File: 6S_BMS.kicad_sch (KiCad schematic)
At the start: 42 parts, among them J1 Conn_01x08_Pin, J4 Conn_01x02_Pin, J5 Conn_01x04_Pin, J6 Conn_01x04_Pin, SW1 SW_SPST, U1 BQ76925RGER, U2 STM32L431KCUx, U3 TJA1051TK-3, U4 TCAN3404DRBRQ1

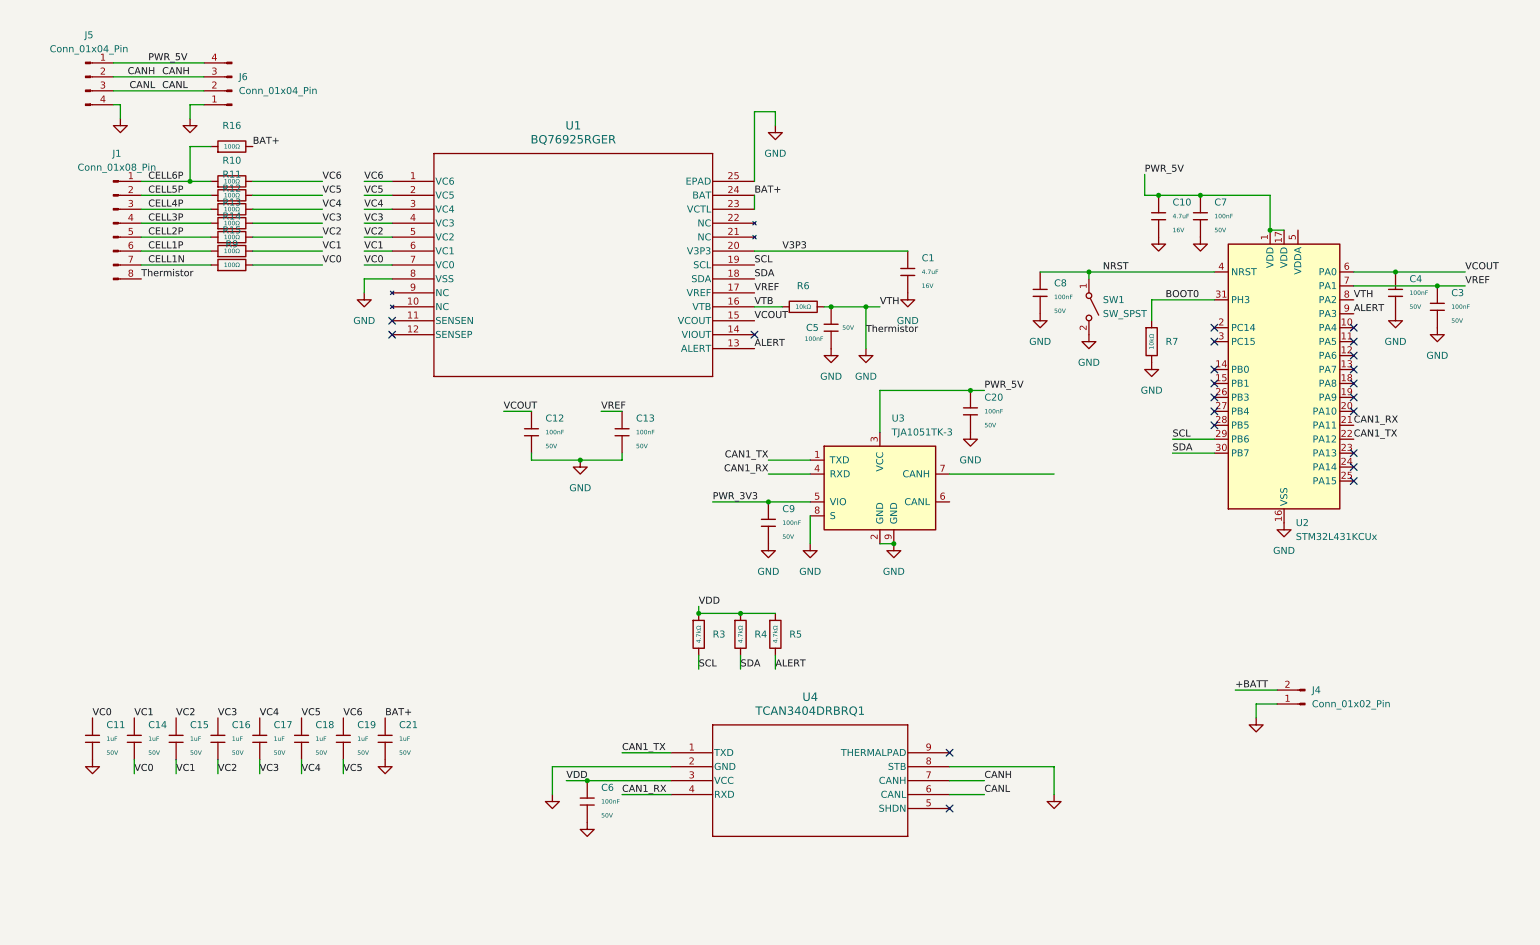
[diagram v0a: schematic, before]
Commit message: Added component properties, updated CAN loop
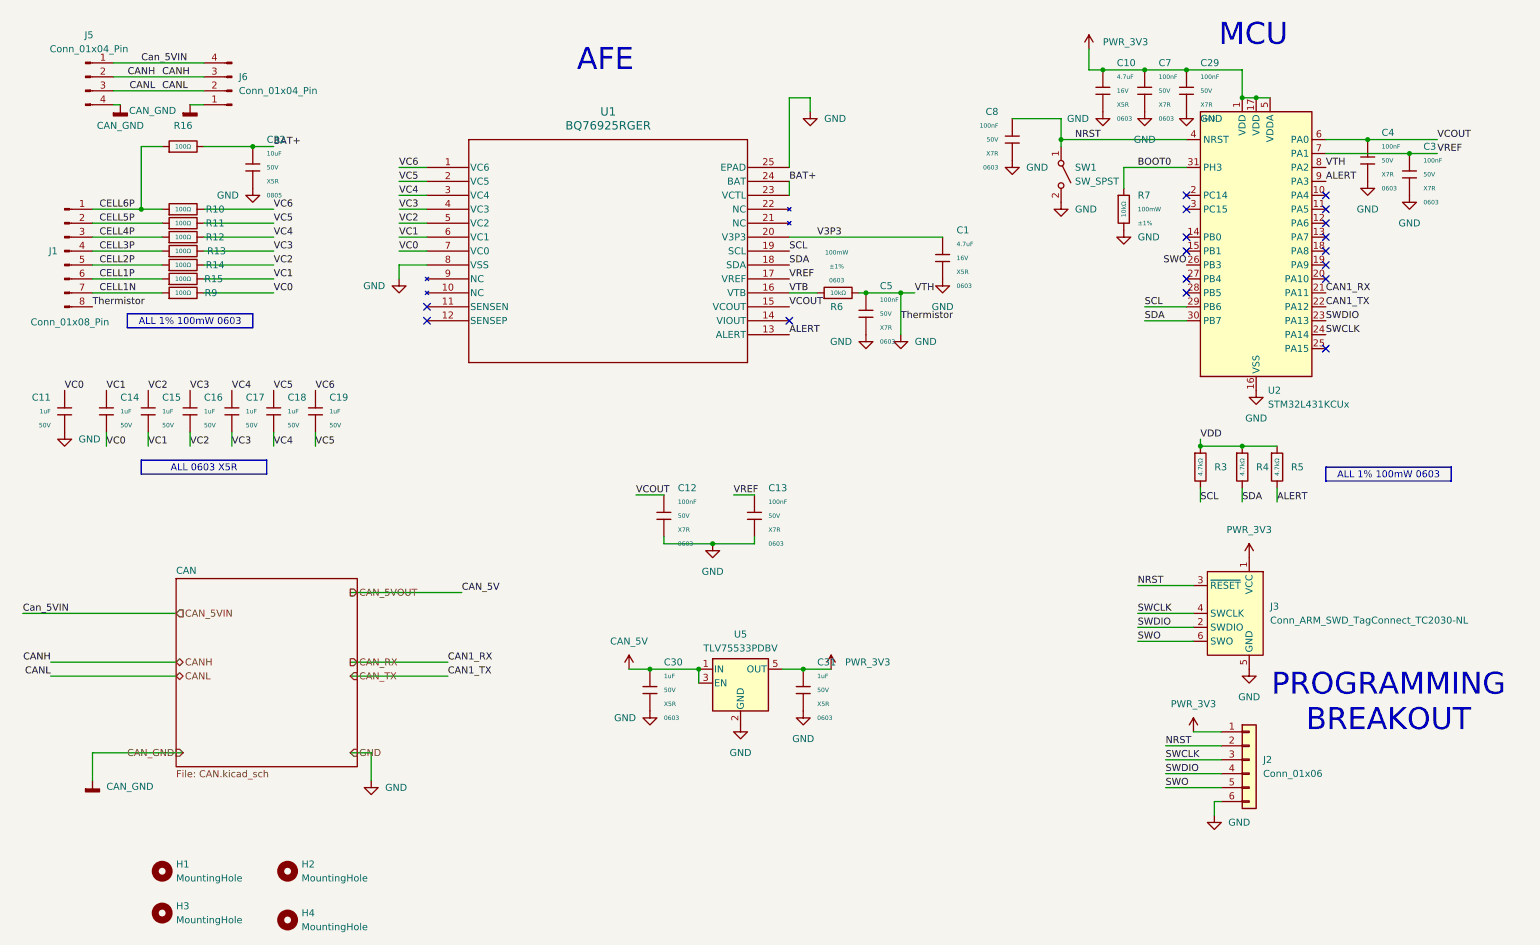
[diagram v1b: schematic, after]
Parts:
- removed C20, C6, C9: 100nF, PCM_JLCPCB:C_0603, symbol PCM_JLCPCB-Capacitors:0603,100nF
- removed C21: 1uF, PCM_JLCPCB:C_0603, symbol PCM_JLCPCB-Capacitors:0603,1uF
- removed J4: Conn_01x02_Pin, symbol Connector:Conn_01x02_Pin
- removed U3: TJA1051TK-3, Package_DFN_QFN:DFN-8-1EP_3x3mm_P0.65mm_EP1.55x2.4mm, symbol Interface_CAN_LIN:TJA1051TK-3
- removed U4: TCAN3404DRBRQ1, TCAN:SON8_DRB_TEX, symbol 2026-03-12_01-27-55:TCAN3404DRBRQ1
- added C29: 100nF, PCM_JLCPCB:C_0603, symbol PCM_JLCPCB-Capacitors:0603,100nF
- added C30, C31: 1uF, PCM_JLCPCB:C_0603, symbol PCM_JLCPCB-Capacitors:0603,1uF
- added C32: 10uF, PCM_JLCPCB:C_0805, symbol PCM_JLCPCB-Capacitors:0805,10uF,(2)
- added H1, H2, H3, H4: MountingHole, symbol Mechanical:MountingHole
- added J2: Conn_01x06, symbol Connector_Generic:Conn_01x06
- added J3: Conn_ARM_SWD_TagConnect_TC2030-NL, Connector:Tag-Connect_TC2030-IDC-NL_2x03_P1.27mm_Vertical, symbol Connector:Conn_ARM_SWD_TagConnect_TC2030-NL
- added U5: TLV75533PDBV, Package_TO_SOT_SMD:SOT-23-5, symbol Regulator_Linear:TLV75533PDBV
- C1, C10, C12, C13, C3, C4, C5, C7, C8, R6: Package (none) -> 0603
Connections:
- net BAT+: now also C32.1
- net GND: now also C29.1, C30.2, C31.2, C32.2, J2.6 (Pin_6), J3.5 (GND), U5.2 (GND); no longer J5.4 (Pin_4), J6.1 (Pin_1)
- net NRST: now also J2.2 (Pin_2), J3.3 (~{RESET})
- net PWR_3V3: now also C10.1, C7.2, U2.1 (VDD), U2.17 (VDD), U2.5 (VDDA), C29.2, C31.1, J2.1 (Pin_1), J3.1 (VCC), U5.5 (OUT)
- net SWDIO: now reaches U2.23 (PA13)
- net SWDIO: now also J2.4 (Pin_4), J3.2 (SWDIO)
- net SWCLK: now reaches U2.24 (PA14)
- net SWCLK: now also J2.3 (Pin_3), J3.4 (SWCLK)
- net SWO: now reaches U2.26 (PB3)
- net SWO: now also J2.5 (Pin_5), J3.6 (SWO)
- net CAN1_RX renamed CAN_RX
- net CAN1_TX renamed CAN_TX
- removed net PWR_5V: C10.1, C7.2, J5.1 (Pin_1), J6.4 (Pin_4), U2.1 (VDD), U2.17 (VDD)
- new net CAN_5V: C30.1, U5.1 (IN), U5.3 (EN)
- new net CAN_5VIN: J5.1 (Pin_1), J6.4 (Pin_4)
- new net CAN_GND: J5.4 (Pin_4), J6.1 (Pin_1)
- no-connect marks 22 -> 17
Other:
- added sheet CAN (CAN.kicad_sch)
- note added: "AFE"
- note added: "MCU"
- note added: "PROGRAMMING BREAKOUT"
- moved on the sheet: C1, C10, C11, C12, C13, C14, C15, C16, C17, C18, C19, C3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
